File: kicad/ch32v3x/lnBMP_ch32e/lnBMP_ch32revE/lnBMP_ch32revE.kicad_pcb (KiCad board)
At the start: 2 copper layers, 51 x 33.3 mm, 43 parts, among them J1 BMP Debug1, J2 BMP Debug2, J3 Debug port, J4 USB_C_Receptacle, U1 CH32V303RCT6, U2 LM1117-3.3, Y1 Crystal, x2 PinSocket_1x03_P1.00mm_Vertic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

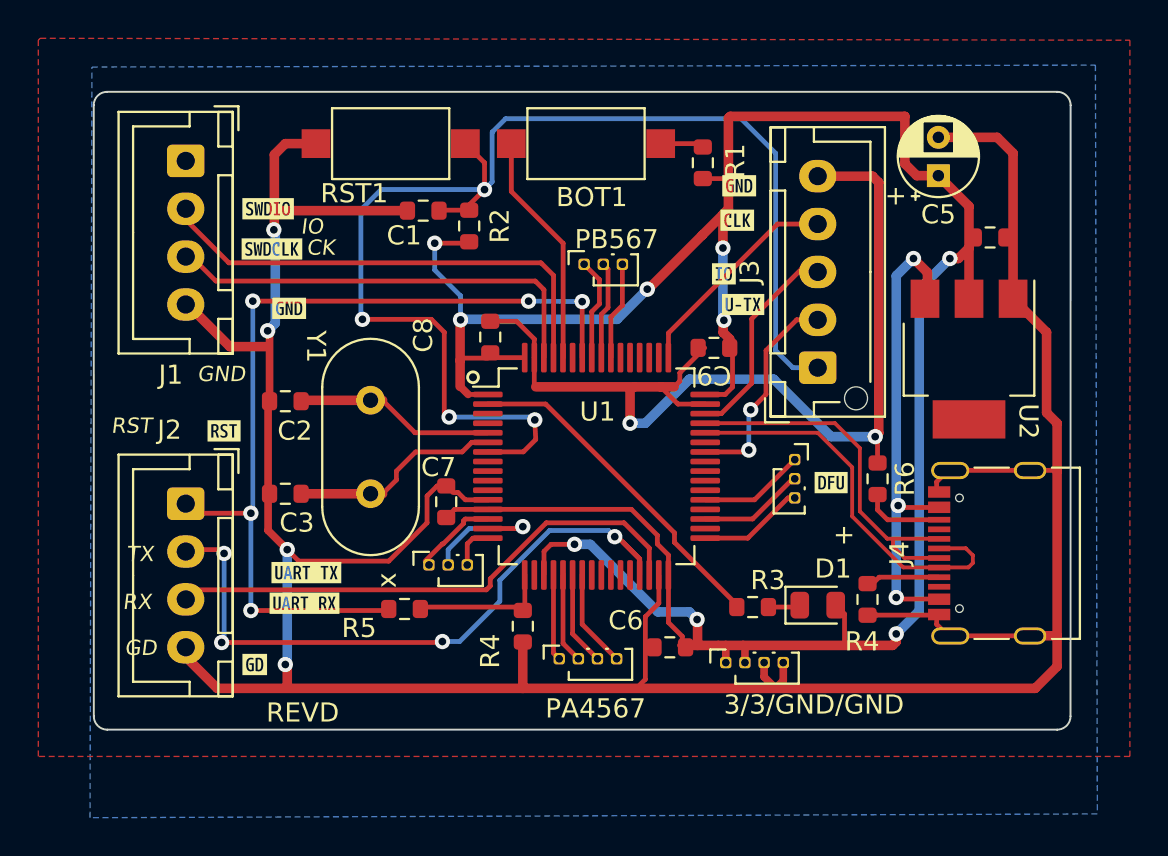
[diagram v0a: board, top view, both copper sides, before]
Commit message: kicad : cleanup ch32 pcb
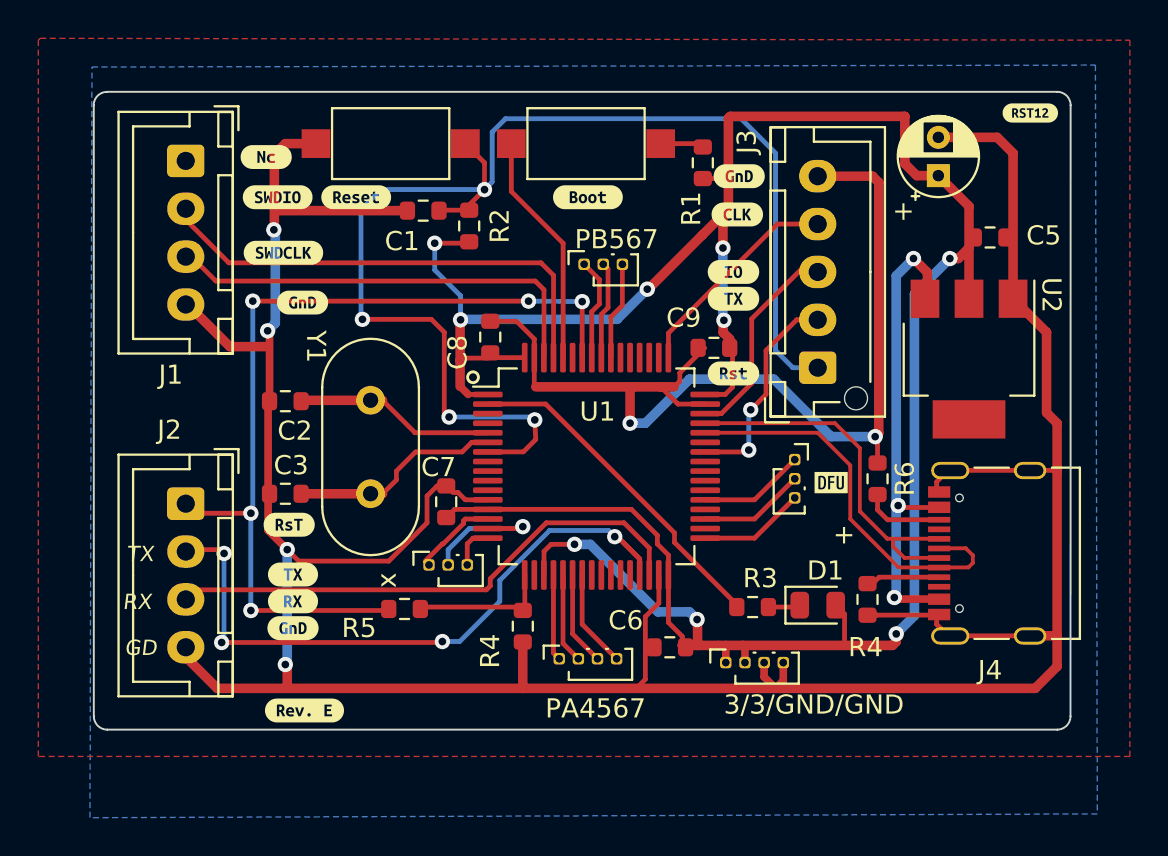
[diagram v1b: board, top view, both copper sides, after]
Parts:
- removed kibuzzard-6534F5CB: G***, kibuzzard-6534F5CB
- removed kibuzzard-6534F635: G***, kibuzzard-6534F635
- removed kibuzzard-6534F652: G***, kibuzzard-6534F652
- removed kibuzzard-6534F67C: G***, kibuzzard-6534F67C
- removed kibuzzard-6534F68E: G***, kibuzzard-6534F68E
- removed kibuzzard-6534F6A3: G***, kibuzzard-6534F6A3
- removed kibuzzard-6534F6BC: G***, kibuzzard-6534F6BC
- removed kibuzzard-6534F8DC: G***, kibuzzard-6534F8DC
- removed kibuzzard-6534F8F1: G***, kibuzzard-6534F8F1
- removed kibuzzard-6534F8FD: G***, kibuzzard-6534F8FD
- removed kibuzzard-6534F90C: G***, kibuzzard-6534F90C
- added kibuzzard-65C13741: G***, kibuzzard-65C13741, F.Cu at (153.2, 68.0)
- added kibuzzard-65C1C718: G***, kibuzzard-65C1C718, F.Cu at (114.7, 93.5)
- added kibuzzard-65C1C729: G***, kibuzzard-65C1C729, F.Cu at (114.7, 92.1)
- added kibuzzard-65C1C789: G***, kibuzzard-65C1C789, F.Cu at (115.2, 77.9)
- added kibuzzard-65C1C789: G***, kibuzzard-65C1C789, F.Cu at (138.0, 71.3)
- added kibuzzard-65C1C789: G***, kibuzzard-65C1C789, F.Cu at (114.7, 94.9)
- added kibuzzard-65C1C7A6: G***, kibuzzard-65C1C7A6, F.Cu at (114.5, 89.5)
- added kibuzzard-65C1C7F5: G***, kibuzzard-65C1C7F5, F.Cu at (113.9, 72.4)
- added kibuzzard-65C1C805: G***, kibuzzard-65C1C805, F.Cu at (114.2, 75.3)
- added kibuzzard-65C1C86E: G***, kibuzzard-65C1C86E, F.Cu at (113.3, 70.3)
- added kibuzzard-65C1C8EE: G***, kibuzzard-65C1C8EE, F.Cu at (137.9, 73.3)
- added kibuzzard-65C1C918: G***, kibuzzard-65C1C918, F.Cu at (137.7, 76.3)
- added kibuzzard-65C1C92F: G***, kibuzzard-65C1C92F, F.Cu at (137.7, 77.7)
- added kibuzzard-65C1C972: G***, kibuzzard-65C1C972, F.Cu at (137.7, 81.6)
- added kibuzzard-65C1C9D7: G***, kibuzzard-65C1C9D7, F.Cu at (118.0, 72.4)
- added kibuzzard-65C1C9E5: G***, kibuzzard-65C1C9E5, F.Cu at (130.1, 72.4)
- added kibuzzard-65C1CA07: G***, kibuzzard-65C1CA07, F.Cu at (115.3, 99.2)
- PB567: value PinSocket_1x03_P1.00mm_Vertical -> PIN1X3
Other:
- board text removed: "CK"
- board text removed: "GND"
- board text removed: "IO"
- board text removed: "REVD"
- board text removed: "RST"

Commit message: kicad  : update (cosmetic)
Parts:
- removed kibuzzard-65C1CA07: G***, kibuzzard-65C1CA07
- added kibuzzard-65C2815C: G***, kibuzzard-65C2815C, F.Cu at (118.7, 99.1)
- added kibuzzard-65C281E1: G***, kibuzzard-65C281E1, F.Cu at (129.4, 99.1)
- added kibuzzard-65C281F8: G***, kibuzzard-65C281F8, F.Cu at (139.1, 99.1)
- added kibuzzard-65C283CB: G***, kibuzzard-65C283CB, F.Cu at (130.2, 74.1)
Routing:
- net GND: track 217.5 -> 221.8 mm, vias 6 -> 8
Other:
- board text removed: "GD"
- board text removed: "RX"
- board text removed: "TX"
